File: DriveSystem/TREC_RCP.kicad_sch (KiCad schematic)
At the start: 5 parts, among them J1 Raspberry_Pi_4

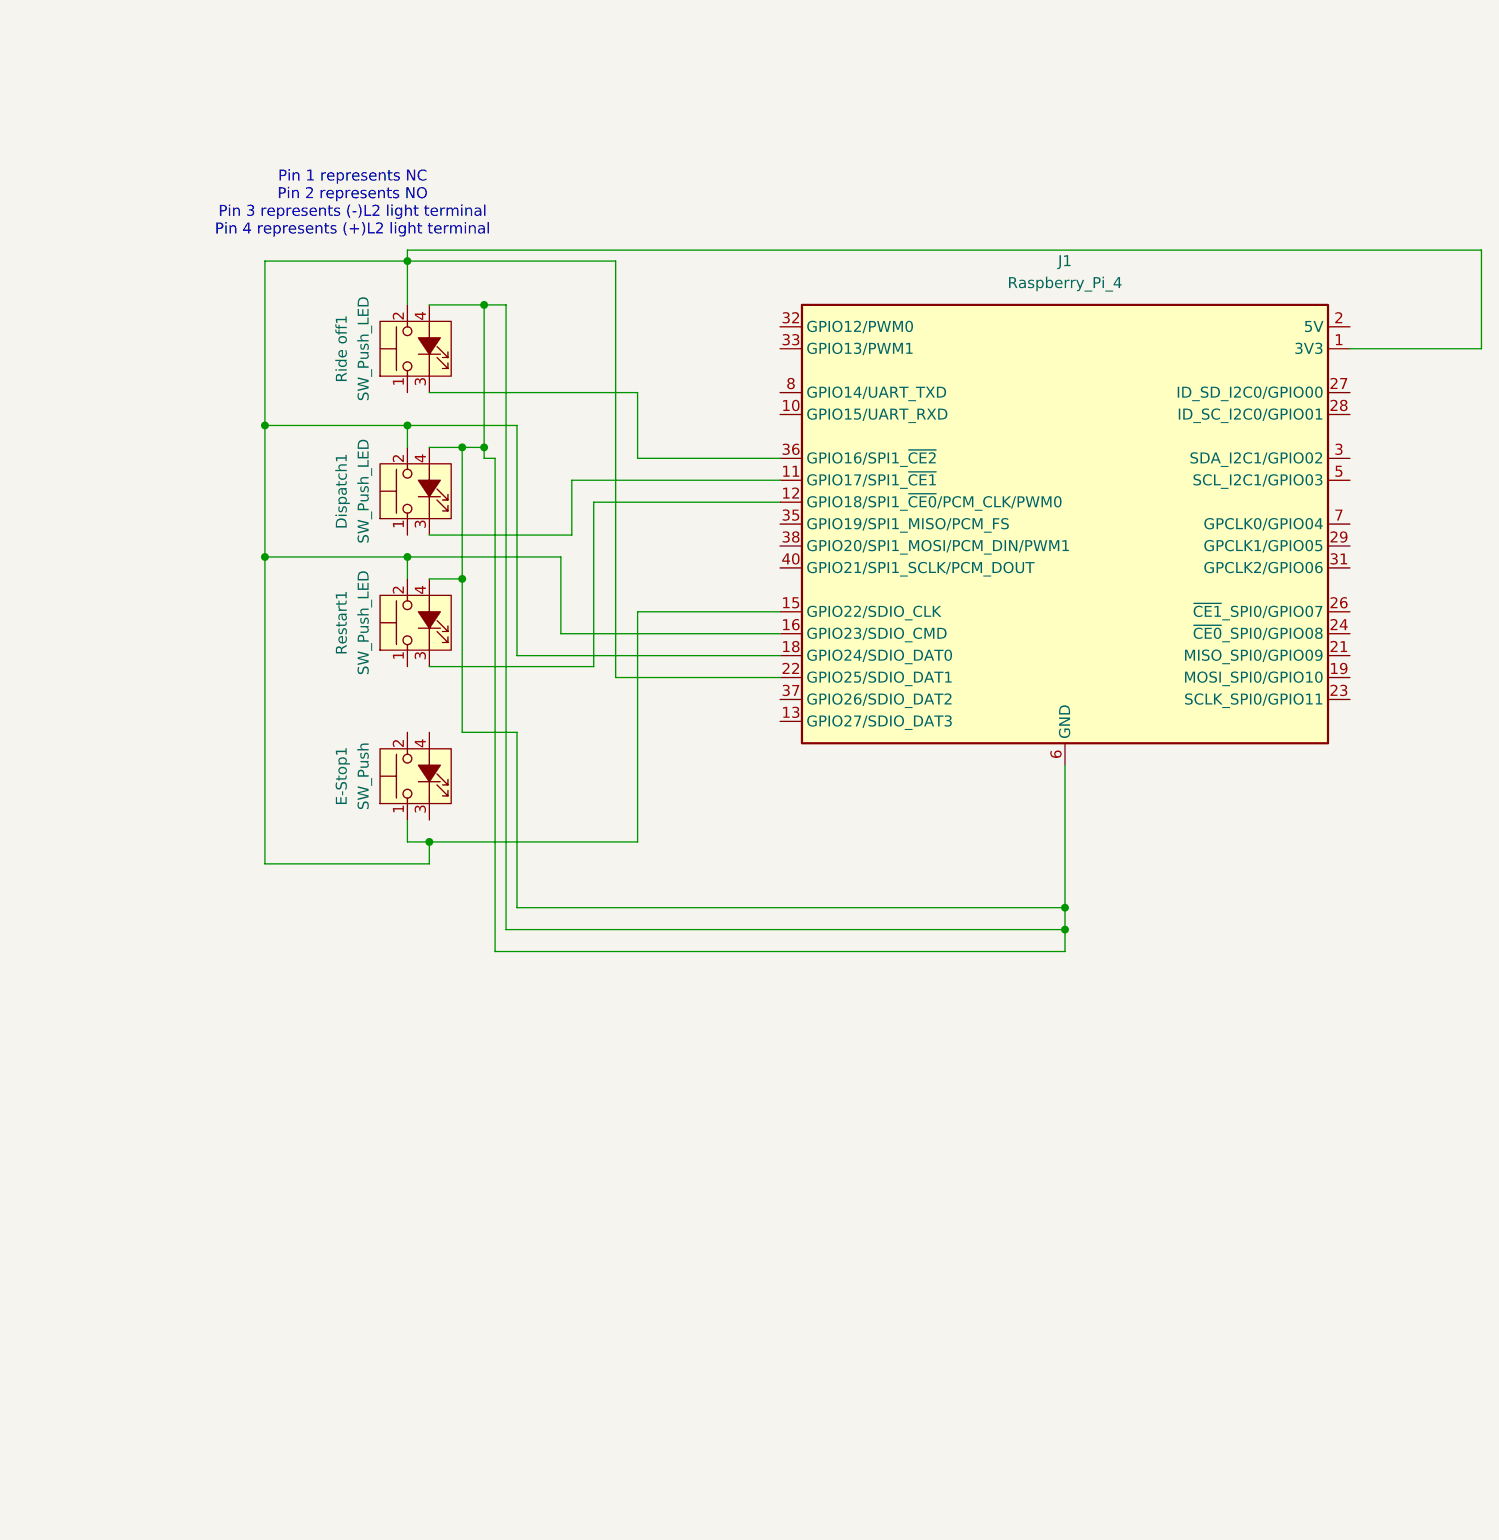
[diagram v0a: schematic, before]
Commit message: Update TREC_RCP.kicad_sch
updated to better reflect our actual switches and connected the estop pin to the pin you told me to
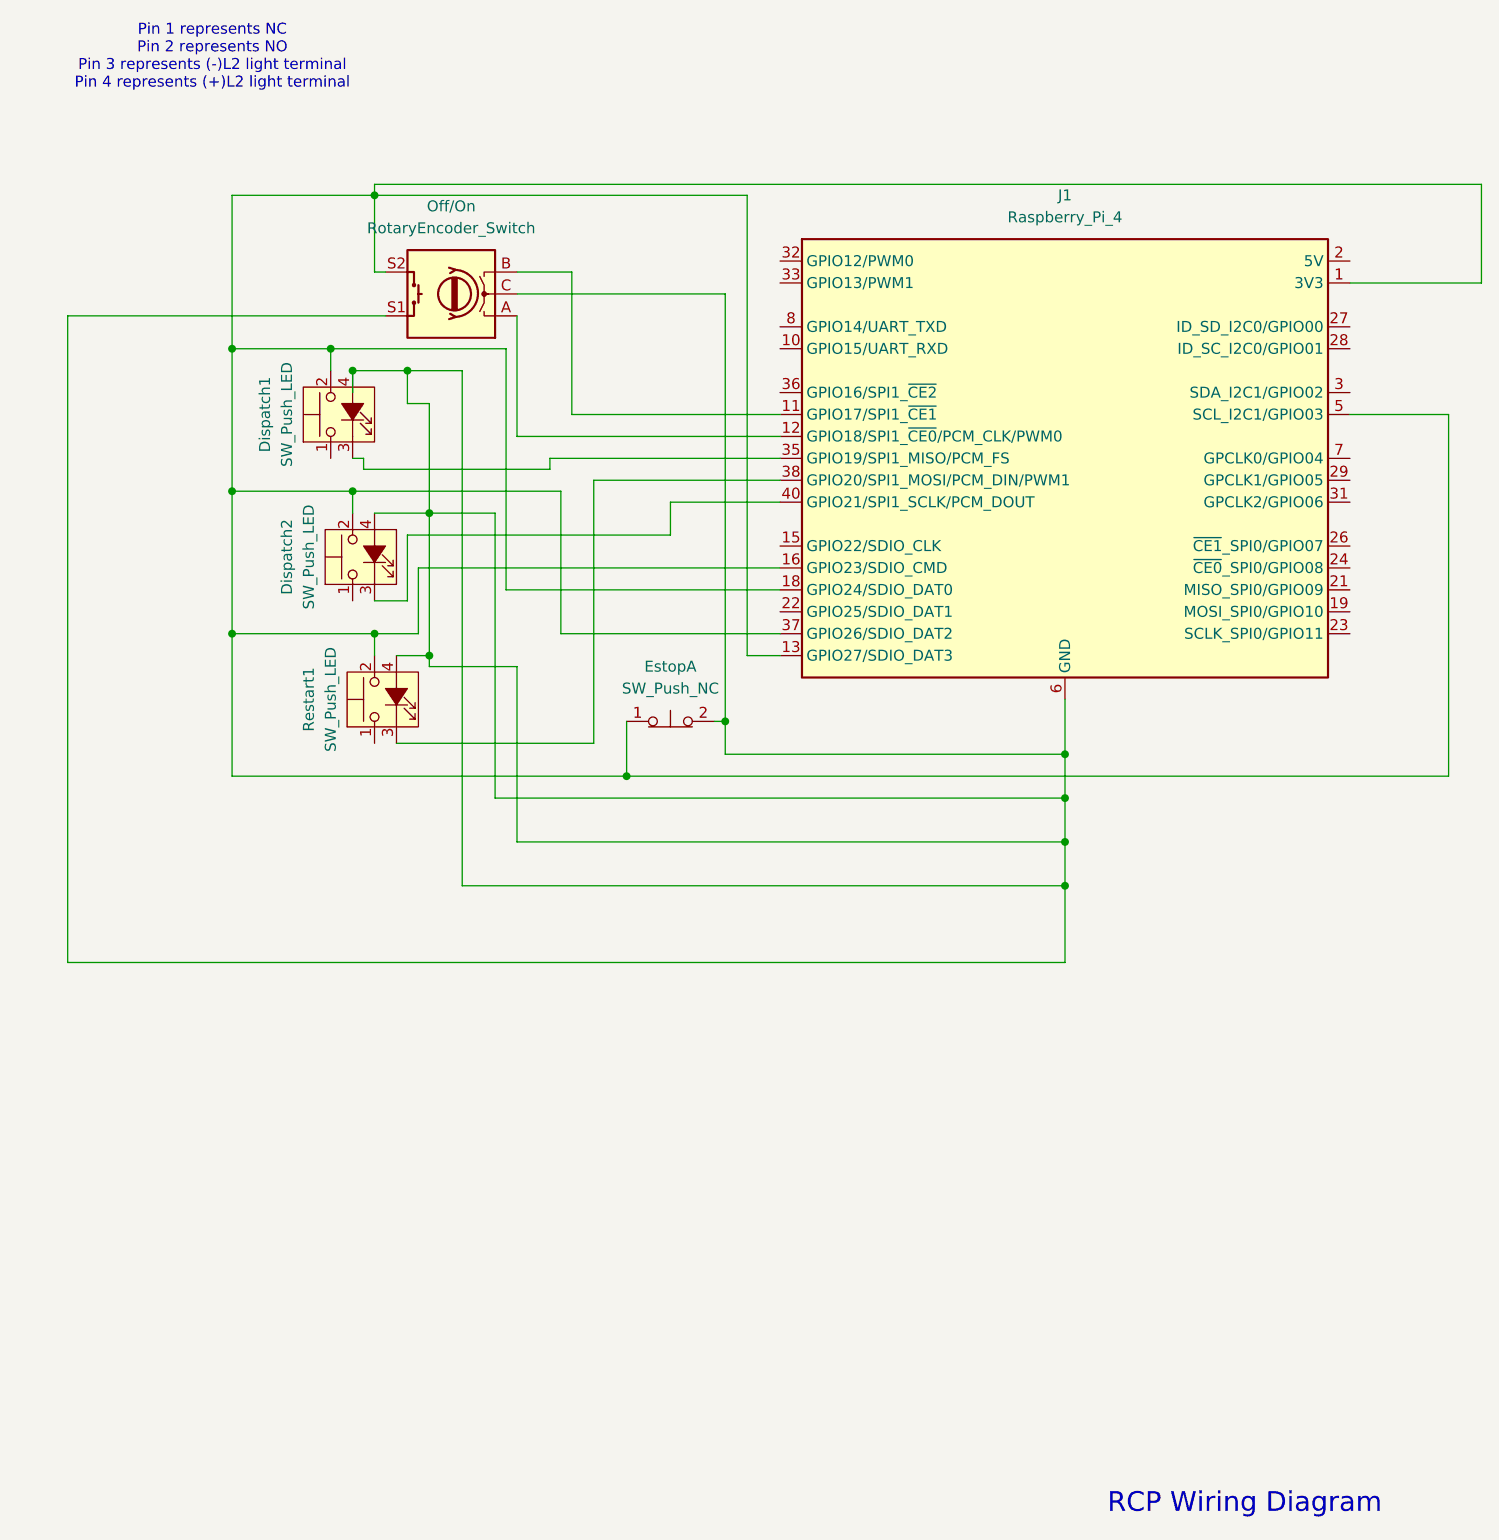
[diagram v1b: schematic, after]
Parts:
- removed E-Stop1: SW_Push, symbol Switch:SW_Push_LED
- removed Ride off1: SW_Push_LED, symbol Switch:SW_Push_LED
- added Dispatch2: SW_Push_LED, symbol Switch:SW_Push_LED
- added Estop: SW_Push_NC, symbol Switch:SW_Push_Open_Dual_x2
- added Off/On: RotaryEncoder_Switch, symbol Device:RotaryEncoder_Switch
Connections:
- net at Dispatch1.2, J1.1 (3V3), J1.16 (GPIO23/SDIO_CMD)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: now also J1.13 (GPIO27/SDIO_DAT3), J1.37 (GPIO26/SDIO_DAT2), J1.5 (SCL_I2C1/GPIO03), Dispatch2.2, Estop.1, Off/On.S2; no longer J1.15 (GPIO22/SDIO_CLK), J1.22 (GPIO25/SDIO_DAT1)
- net at J1.11 (GPIO17/SPI1_~{CE1}): now also Off/On.B; no longer Dispatch1.3 (K)
- net at J1.12 (GPIO18/SPI1_~{CE0}/PCM_CLK/PWM0): now also Off/On.A; no longer Restart1.3 (K)
- net at Dispatch1.4 (A), J1.14 (GND), J1.20 (GND)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: now also Dispatch2.4 (A), Estop.2, Off/On.C, Off/On.S1
- net at J1.35 (GPIO19/SPI1_MISO/PCM_FS): now also Dispatch1.3 (K)
- net at J1.38 (GPIO20/SPI1_MOSI/PCM_DIN/PWM1): now also Restart1.3 (K)
- net at J1.40 (GPIO21/SPI1_SCLK/PCM_DOUT): now also Dispatch2.3 (K)
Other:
- note added: "RCP Wiring Diagram"
- moved on the sheet: Dispatch1, J1, Restart1
